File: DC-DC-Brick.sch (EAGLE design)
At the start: 20 parts

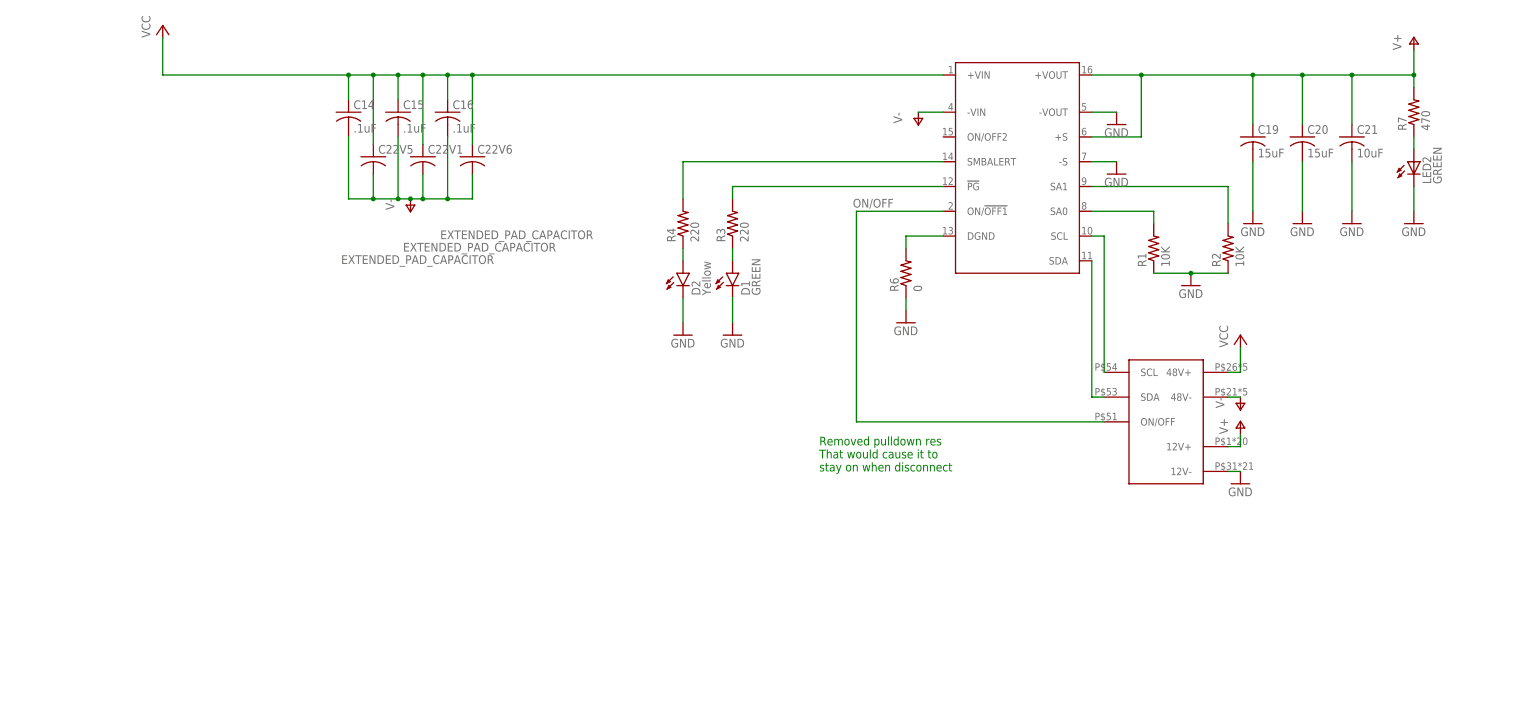
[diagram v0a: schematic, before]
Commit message: Power brick connectors edited
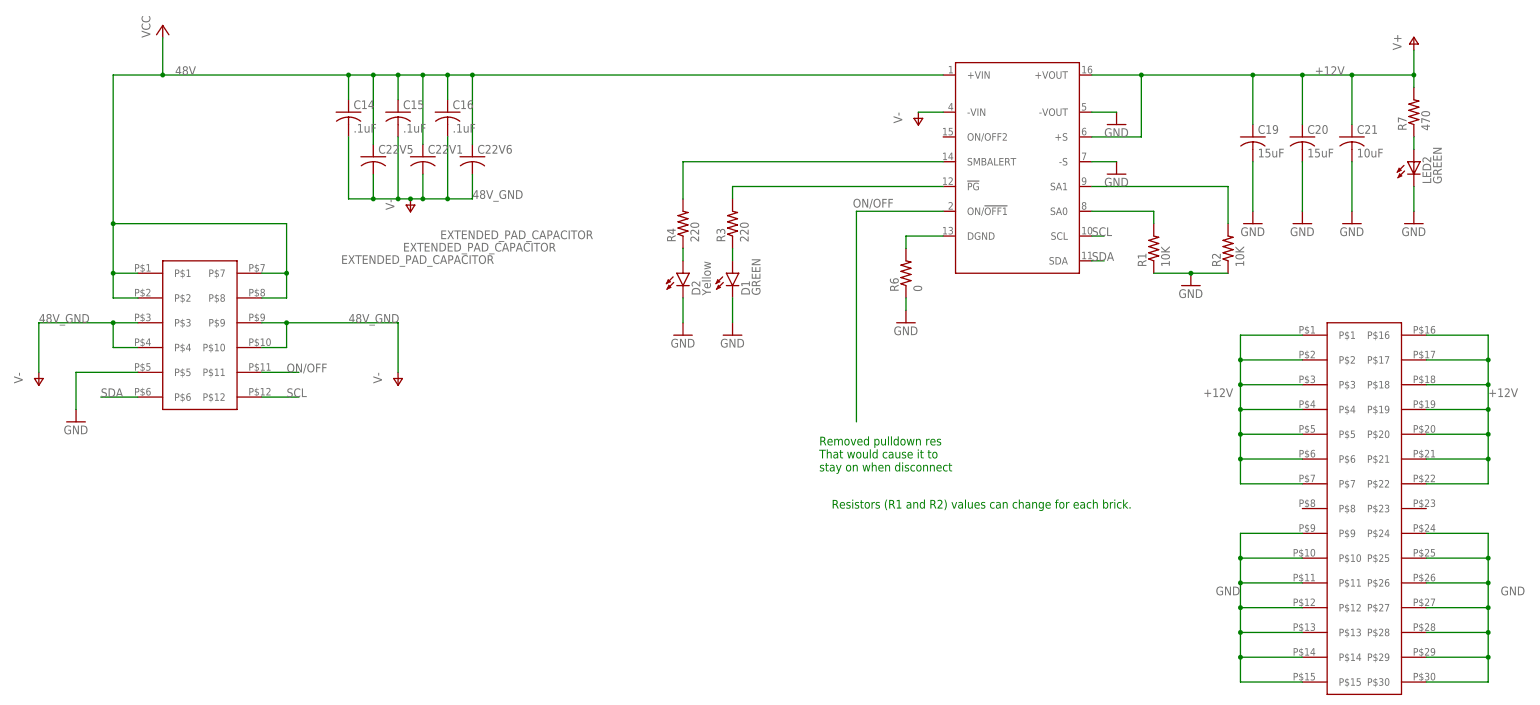
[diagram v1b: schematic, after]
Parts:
- added U$2: POWER_BRICK_CONNECTORS(2X6), MotherBoardParts2:POWER_BRICK_CONNECTORS(2X6)
- U$3: value POWER-BRICK-CONNECTOR -> POWER_BRICK_CONNECTORS(2X15); device MotherboardParts:POWER-BRICK-CONNECTOR -> MotherBoardParts2:POWER_BRICK_CONNECTORS(2X15)
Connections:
- removed net N$10: U$1.SCL, U$3.SCL
- removed net N$8: U$1.SDA, U$3.SDA
- removed net V+: C19.1, C20.1, C21.1, R7.2, U$1.+S, U$1.+VOUT, U$3.12V+
- removed net VCC: C14.1, C15.1, C16.1, C22V1.3, C22V5.3, C22V6.3, U$1.+VIN, U$3.48V+
- new net +12V: C19.1, C20.1, C21.1, R7.2, U$1.+S, U$1.+VOUT, U$3.P$1, U$3.P$16, U$3.P$17, U$3.P$18, U$3.P$19, U$3.P$2, U$3.P$20, U$3.P$21, U$3.P$22, U$3.P$3, U$3.P$4, U$3.P$5, U$3.P$6, U$3.P$7
- new net 48V: C14.1, C15.1, C16.1, C22V1.3, C22V5.3, C22V6.3, U$1.+VIN, U$2.P$1, U$2.P$2, U$2.P$7, U$2.P$8
- new net 48V_GND: C14.2, C15.2, C16.2, C22V1.4, C22V5.4, C22V6.4, U$2.P$10, U$2.P$3, U$2.P$4, U$2.P$9
- new net SCL: U$1.SCL, U$2.P$12
- new net SDA: U$1.SDA, U$2.P$6
- net GND: now also U$2.P$5, U$3.P$10, U$3.P$11, U$3.P$12, U$3.P$13, U$3.P$14, U$3.P$15, U$3.P$24, U$3.P$25, U$3.P$26, U$3.P$27, U$3.P$28, U$3.P$29, U$3.P$30, U$3.P$9; no longer U$3.12V-
- net ON/OFF: now also U$2.P$11; no longer U$3.ON/OFF
- net V-: no longer C14.2, C15.2, C16.2, C22V1.4, C22V5.4, C22V6.4, U$3.48V-
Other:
- note added: "Resistors (R1 and R2) values can change for each brick."

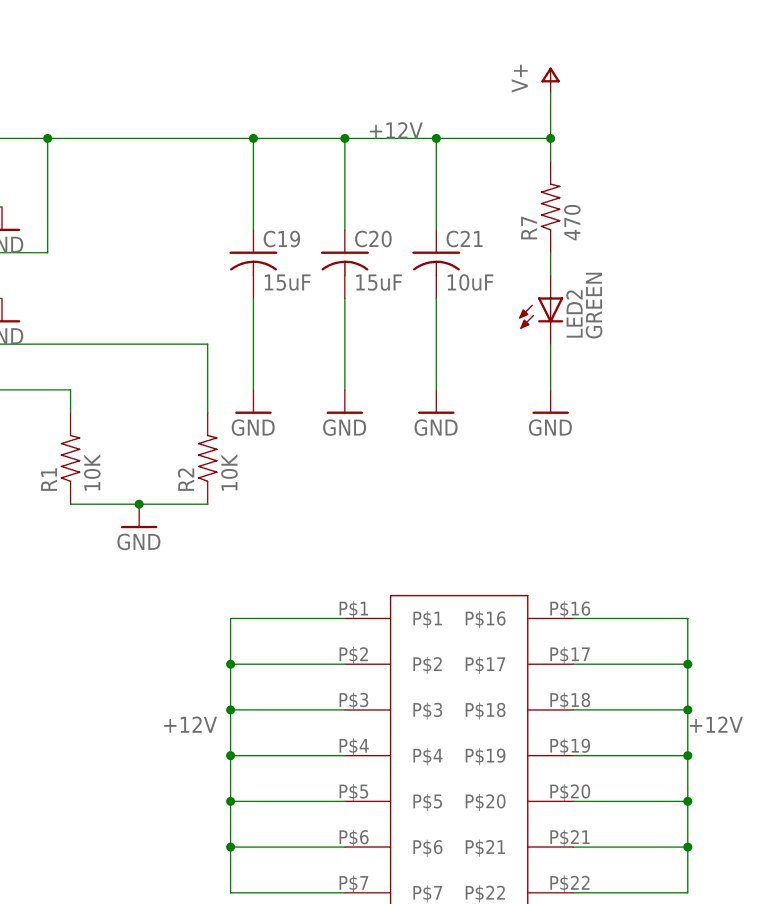
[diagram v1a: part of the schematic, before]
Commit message: New power brick board
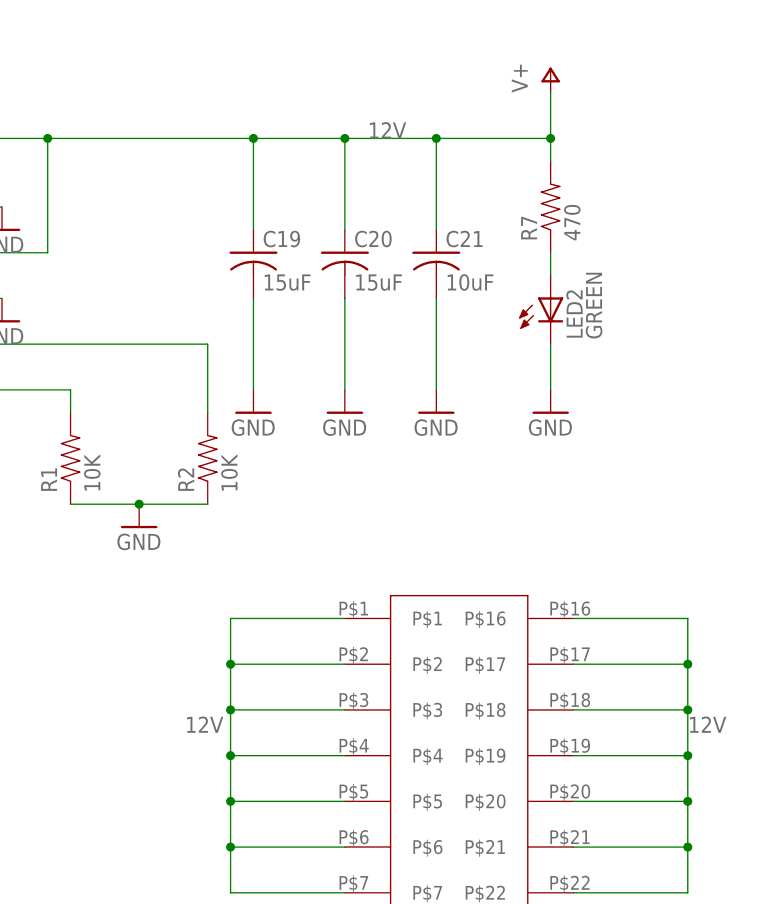
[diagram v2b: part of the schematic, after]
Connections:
- net +12V renamed 12V
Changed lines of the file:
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@@
 <?xml version="1.0" encoding="utf-8"?>
 <!DOCTYPE eagle SYSTEM "eagle.dtd">
-<eagle version="8.3.2">
+<eagle version="8.4.2">
 <drawing>
 <settings>
@@
 <class number="0" name="default" width="0" drill="0">
 </class>
+<class number="1" name="I2C" width="0.254" drill="0">
+</class>
 </classes>
 <parts>
@@
 </segment>
 </net>
-<net name="+12V" class="0">
+<net name="12V" class="0">
 <segment>
 <wire x1="327.66" y1="162.56" x2="327.66" y2="160.02" width="0.1524" layer="91"/>
@@
 <pinref part="U$3" gate="G$1" pin="P$7"/>
 <wire x1="292.1" y1="78.74" x2="304.8" y2="78.74" width="0.1524" layer="91"/>
-<label x="284.48" y="96.52" size="1.778" layer="95"/>
-</segment>
-<segment>
+<label x="287.02" y="96.52" size="1.778" layer="95"/>
+</segment>
+<segment>

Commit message: Edit Signal Name
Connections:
- removed net V-: U$1.-VIN
- net 48V_GND: now also U$1.-VIN
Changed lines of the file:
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@@
 <?xml version="1.0" encoding="utf-8"?>
 <!DOCTYPE eagle SYSTEM "eagle.dtd">
-<eagle version="8.4.2">
+<eagle version="8.4.1">
 <drawing>
 <settings>
@@
 </segment>
 </net>
-<net name="V-" class="0">
-<segment>
-<pinref part="U$1" gate="G$1" pin="-VIN"/>
-<wire x1="231.14" y1="154.94" x2="226.06" y2="154.94" width="0.1524" layer="91"/>
-<pinref part="P-2" gate="1" pin="V-"/>
-</segment>
-</net>
 <net name="N$12" class="0">
 <segment>
@@
 <label x="45.72" y="111.76" size="1.778" layer="95"/>
 </segment>
-</net>
+<segment>
+<pinref part="U$1" gate="G$1" pin="-VIN"/>
+<wire x1="231.14" y1="154.94" x2="226.06" y2="154.94" width="0.1524" layer="91"/>
+<pinref part="P-2" gate="1" pin="V-"/>
+</segment>
+</net>
